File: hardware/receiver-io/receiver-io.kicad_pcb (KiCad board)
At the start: 2 copper layers, 68.6 x 53.3 mm, 20 parts, among them J1 Input

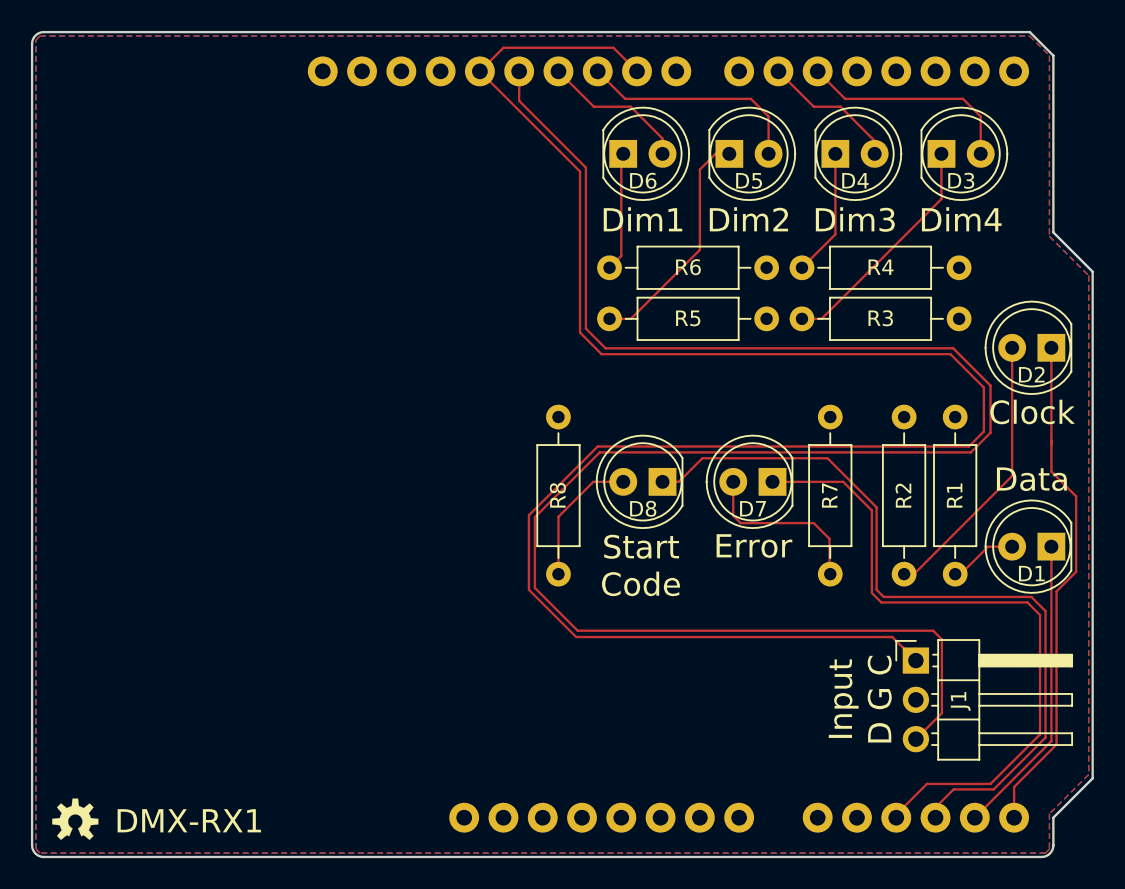
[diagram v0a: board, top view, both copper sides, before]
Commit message: Prototype version of DMX, Analog, and PWM IO Modules and both TX and RX IO interfaces.
Make io-analog a stackable family
io-analog-core handles D to A
io-analog-voltage handles voltage output
io-analog-pwm handles pwm output for leds, drive display pro

Refactor display-pro to work with io-analog-pwm
Add correct coax power connector

Move TX2 to tx-io
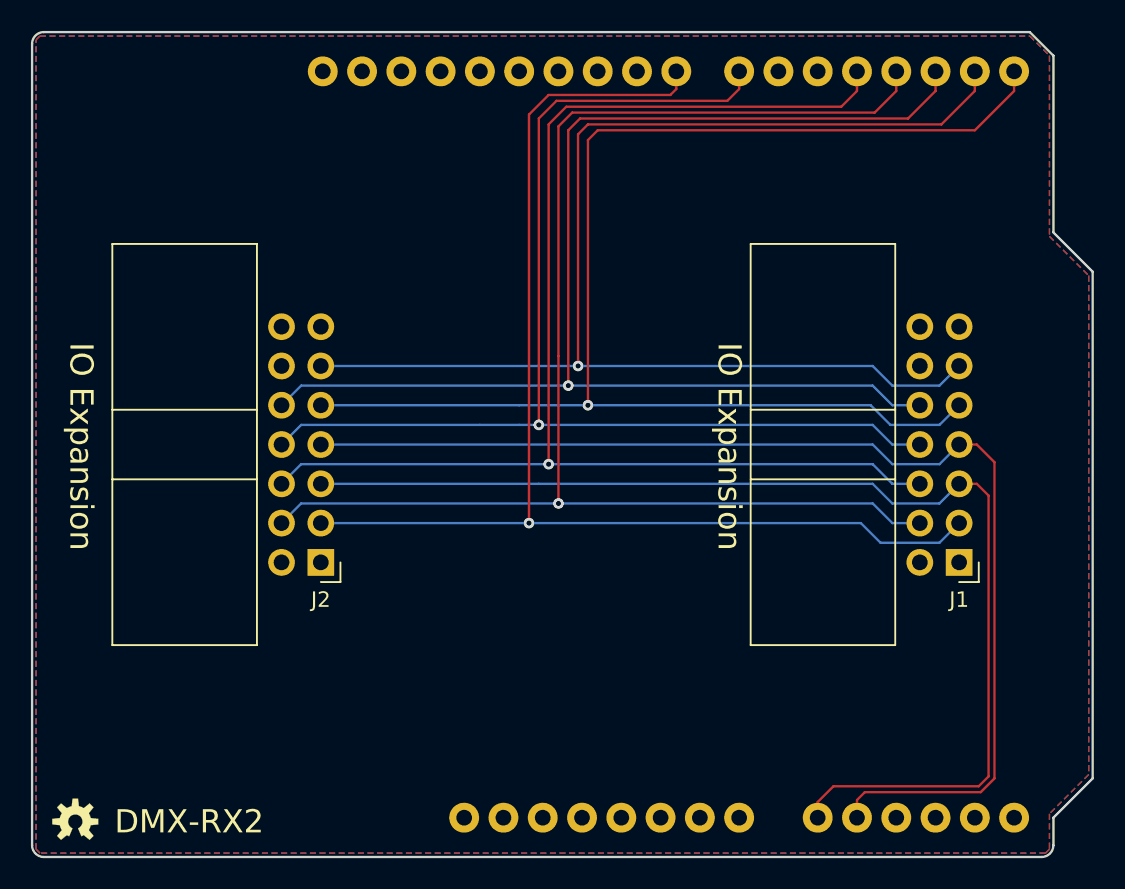
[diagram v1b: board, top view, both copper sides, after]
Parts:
- removed D1: DATA, LED_THT:LED_D5.0mm
- removed D2: CLOCK, LED_THT:LED_D5.0mm
- removed D3: DIM3, LED_THT:LED_D5.0mm
- removed D4: DIM2, LED_THT:LED_D5.0mm
- removed D5: DIM1, LED_THT:LED_D5.0mm
- removed D6: DIM0, LED_THT:LED_D5.0mm
- removed D7: ERROR, LED_THT:LED_D5.0mm
- removed D8: START_CODE, LED_THT:LED_D5.0mm
- removed R1, R2, R3, R4, R5, R6, R7, R8: 330, Resistor_THT:R_Axial_DIN0207_L6.3mm_D2.5mm_P10.16mm_Horizontal
- added J2: IO EXTENSION, Connector_IDC:IDC-Header_2x07_P2.54mm_Horizontal, F.Cu at (135.0, 97.5)
- J1: value Input -> IO EXTENSION; footprint Connector_PinHeader_2.54mm:PinHeader_1x03_P2.54mm_Horizontal -> Connector_IDC:IDC-Header_2x07_P2.54mm_Horizontal
- moved J1 6.94 mm to (176.3, 97.5), turned to 180 degrees
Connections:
- A1 pad 10: Net-(A1-Pad10) -> /A1
- A1 pad 11: /~ERR -> Net-(A1-Pad11)
- A1 pad 12: /~SC -> Net-(A1-Pad12)
- A1 pad 13: /~DATA -> Net-(A1-Pad13)
- A1 pad 14: /~CLOCK -> Net-(A1-Pad14)
- A1 pad 15: Net-(A1-Pad15) -> /DMX-RX
- A1 pad 16: Net-(A1-Pad16) -> /DMX-TX
- A1 pad 17: Net-(A1-Pad17) -> /DMX-DIR
- A1 pad 18: Net-(A1-Pad18) -> /SR-OUT
- A1 pad 19: Net-(A1-Pad19) -> /SR-CLK
- A1 pad 20: /~DIM3 -> Net-(A1-Pad20)
- A1 pad 21: /~DIM2 -> Net-(A1-Pad21)
- A1 pad 22: Net-(A1-Pad22) -> /~SR_CLR
- A1 pad 23: Net-(A1-Pad23) -> /~WR
- A1 pad 24: /RXCLK -> Net-(A1-Pad24)
- A1 pad 25: /~DIM1 -> Net-(A1-Pad25)
- A1 pad 26: /~DIM0 -> Net-(A1-Pad26)
- A1 pad 27: /RX -> Net-(A1-Pad27)
- A1 pad 28: /RXCLK -> Net-(A1-Pad28)
- A1 pad 9: Net-(A1-Pad9) -> /A0
- J1 pad 1: /RXCLK -> +5V
- J1 pad 2: GND -> +5V
- J1 pad 3: /RX -> /~WR
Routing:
- net /RXCLK: track 126.2 -> 0.00 mm
- net /RX: track 120.3 -> 0.00 mm
- net /SR-OUT: track 0.00 -> 90.8 mm, vias 0 -> 1
- net /DMX-RX: track 0.00 -> 89.6 mm, vias 0 -> 1
- net /SR-CLK: track 0.00 -> 86.4 mm, vias 0 -> 1
- net /DMX-TX: track 0.00 -> 85.4 mm, vias 0 -> 1
- net /DMX-DIR: track 0.00 -> 84.9 mm, vias 0 -> 1
- net /~WR: track 0.00 -> 80.1 mm, vias 0 -> 1
- net /~SR_CLR: track 0.00 -> 77.0 mm, vias 0 -> 1
- net /A1: track 0.00 -> 76.1 mm
- net /A0: track 0.00 -> 75.5 mm
- net /~SC: track 50.4 -> 0.00 mm
- net /~ERR: track 43.4 -> 0.00 mm
- net /~CLOCK: track 33.0 -> 0.00 mm
- net /~DATA: track 19.6 -> 0.00 mm
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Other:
- board text added: "DMX-RX2"
- board text added: "DMX-RX2, Rev 1.1 Crazy Giraffe Software"
- board text added: "IO Expansion"
- board text removed: "Clock"
- board text removed: "D G C"
- board text removed: "DMX-RX1"
- board text removed: "DMX-RX1, Rev 1.3 Crazy Giraffe Software"
- board text removed: "Data"
- board text removed: "Dim1"
- board text removed: "Dim2"
- board text removed: "Dim3"
- board text removed: "Dim4"
- board text removed: "Error"
- board text removed: "Input"
- board text removed: "Start Code"
